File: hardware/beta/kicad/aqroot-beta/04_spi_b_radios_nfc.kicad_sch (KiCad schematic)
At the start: 0 parts

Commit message: AQROOT Beta: capture SPI-B radios and NFC architecture
Completes sheet 04, bringing all three SPI Bus B devices into the
schematic against the functional placeholder symbols added in 5e4471a,
ba2be78 and 1f152bd. Bus B is now the shared SPI_B_SCK / SPI_B_MOSI /
SPI_B_MISO bus with one chip select per device.

CC1101 -- AQROOT_Beta:CC1101_RADIO_PLACEHOLDER
  CC1101_CS_N, CC1101_GDO0, CC1101_RF_TBD, 100nF decoupling,
  10k hardware pull-up on CC1101_CS_N.

SX1262 -- AQROOT_Beta:SX1262_MODULE_PLACEHOLDER
  SX1262_CS_N, SX1262_BUSY, SX1262_DIO1, SX1262_RST_N (from expander
  U60 P01), SX1262_RF_TBD, 100nF decoupling, 10k hardware pull-up on
  SX1262_CS_N.

ST25R3916 -- AQROOT_Beta:ST25R3916_NFC_PLACEHOLDER
  VDD_IO_3V3 and VDD_DIG_3V3 to +3V3, VDD_PA_5V to NFC_5V_PA_PENDING
  (the switched 5V PA rail, boost IC unresolved). NFC_CS_N, NFC_IRQ,
  and the RF and clock ports NFC_RFO1/RFO2/RFI1/RFI2_TBD and
  NFC_XIN/XOUT_TBD. 10k hardware pull-up on NFC_CS_N, plus provisional
  100nF placeholders on +3V3 and on NFC_5V_PA_PENDING.

Passives placed: C16, C17 (100nF), C18, C19 (100nF_PLACEHOLDER),
R27, R28, R29 (10k CS pull-ups).

Root sheet exposes and labels SPI_B_SCK, SPI_B_MOSI, SPI_B_MISO,
CC1101_CS_N, CC1101_GDO0, SX1262_CS_N, SX1262_BUSY, SX1262_DIO1,
SX1262_RST_N, NFC_CS_N and NFC_IRQ.

All three parts carry a blank Footprint and on_board=no, and the sheet
carries DO NOT ROUTE notes. Nothing here is routable: the CC1101
module-vs-bare-IC choice, the SX1262 certified module (Ebyte E22 vs
Waveshare Core1262), and the ST25R3916 package, support networks, coil
and matching all remain unresolved. Every _TBD and _PENDING net name is
deliberate and must be replaced before layout.

Also in this commit, both rewritten by KiCad during the same session:
  - aqroot-Beta.kicad_pro: ERC pin_to_pin severity raised from warning
    to error, and used_designators updated by the annotator.
  - 03_spi_a_display_sd.kicad_sch: two pin UUIDs regenerated on save;
    no connectivity or compon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
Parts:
- added C16, C17: 100nF, symbol Device:C
- added C18, C19: 100nF_PLACEHOLDER, symbol Device:C
- added R27, R28, R29: 10k, symbol Device:R
- added U7: CC1101_RADIO_PLACEHOLDER, symbol AQROOT_Beta:CC1101_RADIO_PLACEHOLDER
- added U8: SX1262_MODULE_PLACEHOLDER, symbol AQROOT_Beta:SX1262_MODULE_PLACEHOLDER
- added U9: ST25R3916_NFC_PLACEHOLDER, symbol AQROOT_Beta:ST25R3916_NFC_PLACEHOLDER
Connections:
- new net +3V3: C16.1, C17.1, C18.1, R27.1, R28.1, R29.1, U7.1 (VCC_3V3), U8.1 (VCC_3V3), U9.1 (VDD_IO_3V3), U9.2 (VDD_DIG_3V3)
- new net CC1101_CS_N: R28.2, U7.6 (CS_N)
- new net CC1101_GDO0: U7.7 (GDO0)
- new net CC1101_RF_TBD: U7.8 (RF_ANT)
- new net GND: C16.2, C17.2, C18.2, C19.2, U7.2 (GND), U8.2 (GND), U9.4 (GND)
- new net NFC_5V_PA_PENDING: C19.1, U9.3 (VDD_PA_5V)
- new net NFC_CS_N: R29.2, U9.8 (CS_N)
- new net NFC_IRQ: U9.9 (IRQ)
- new net NFC_RFI1_TBD: U9.12 (RFI1)
- new net NFC_RFI2_TBD: U9.13 (RFI2)
- new net NFC_RFO1_TBD: U9.10 (RFO1)
- new net NFC_RFO2_TBD: U9.11 (RFO2)
- new net NFC_XIN_TBD: U9.14 (XIN)
- new net NFC_XOUT_TBD: U9.15 (XOUT)
- new net SPI_B_MISO: U7.5 (MISO), U8.5 (MISO), U9.7 (MISO)
- new net SPI_B_MOSI: U7.4 (MOSI), U8.4 (MOSI), U9.6 (MOSI)
- new net SPI_B_SCK: U7.3 (SCK), U8.3 (SCK), U9.5 (SCK)
- new net SX1262_BUSY: U8.7 (BUSY)
- new net SX1262_CS_N: R27.2, U8.6 (CS_N)
- new net SX1262_DIO1: U8.8 (DIO1)
- new net SX1262_RF_TBD: U8.10 (RF_ANT)
- new net SX1262_RST_N: U8.9 (RESET_N)
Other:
- note added: "CC1101 FUNCTIONAL PLACEHOLDER MODULE / BARE-IC IMPLEMENTATION PENDING RF MATCHING / FILTERING / ANTENNA INTERFACE PENDING GDO2 INTENTIONALLY OMITTED CS HAS 10k HARDWARE PULL-UP TO +3V3 NO FOOTPRINT DO NOT ROUTE"
- note added: "SPI BUS B - BETA BRING-UP RISK THREE SHARED DEVICES: CC1101 + SX1262 + ST25R3916 ALL THREE CS LINES HAVE HARDWARE PULL-UPS ST25R3916 WAS VALIDATED STANDALONE ON ALPHA NFC AS THIRD BUS-B DEVICE IS FIRST VALIDATED ON BETA FIRMWARE MUST: - DRIVE ALL CS HIGH BEFORE INITIALIZATION - USE A BUS MUTEX - SET SPI MODE / FREQUENCY PER TRANSACTION - VERIFY NO DEVICE HOLDS MISO DO NOT ROUTE NFC UNTIL PACKAGE,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"
- note added: "SX1262 FUNCTIONAL PLACEHOLDER EXACT CERTIFIED MODULE PENDING EBYTE E22 VS WAVESHARE CORE1262 UNRESOLVED RF / ANTENNA INTERFACE PENDING CS HAS 10k HARDWARE PULL-UP TO +3V3 RESET SAFE-STATE CONTROLLED BY U60 P01 NO FOOTPRINT DO NOT ROUTE"

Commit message: Schematics: root connectivity pass for XGPIO, I2C_SDA_INT and NFC_5V_PA_PENDING
Work-in-progress checkpoint of the root-level connectivity pass. Verified with
kicad-cli netlist and ERC comparison against the previous commit.

Resolved:
- NFC_5V_PA_PENDING was split across two isolated sheet-local nets,
  /01_POWER_TREE/NFC_5V_PA_PENDING (C34.2 C35.1 R44.2 TP9.1 U13.6) and
  /04_SPI_B_RADIOS_NFC/NFC_5V_PA_PENDING (C19.1 alone). Promoted the local
  label in 04_spi_b_radios_nfc to a hierarchical input label, added the
  matching sheet pin on the root, and extended the wire to reach it. These
  now form a single root net /NFC_5V_PA_PENDING with all 6 nodes.
- I2C_SDA_INT: U14.8 was stranded on its own sheet-local net. It now joins
  the main /I2C_SDA_INT net (6 -> 7 nodes).
- ERC pin_not_connected: 77 -> 56 (21 pins newly connected).

Known incomplete, to be finished in a follow-up:
- 18 newly placed root labels are dangling because their wiring is not yet
  drawn: XGPIO0..XGPIO14, ACC_PWR_EN, FAST_IO_U0TXD_ROOTPROBE_CS, WAKE_INT_N.
  ERC label_dangling: 39 -> 57.
- REGRESSION: WAKE_INT_N lost U1.23 (MCU wake input). The root wire from
  (152.4, 24.13) to (152.4, 26.67) was removed, which disconnected the
  WAKE_INT_N label from the 02_MCU_CORE sheet pin at (152.4, 25.4). The net
  dropped from 4 nodes (R3.1 U1.23 U2.1 U3.1) to 3, and U1.23 is now an
  isolated /02_MCU_CORE/WAKE_INT_N. This must be reconnected before the
  netlist is used for layout.

Also clears the stale used_designators cache in the project file, a side
effect of the KiCad editing session.

No symbol, footprint, PCB or library-table changes.

Co-Authored-By: Claude Opus 5 <noreply@anthropic.com>
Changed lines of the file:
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@@
-	(wire
-		(pts
-			(xy 104.14 129.54) (xy 104.14 130.81)
-		)
-		(stroke
-			(width 0)
-			(type default)
-		)
-	)
 	(wire
 		(pts
@@
 		(pts
 			(xy 66.04 52.07) (xy 67.31 52.07)
+		)
+		(stroke
+			(width 0)
+			(type default)
+		)
+	)
+	(wire
+		(pts
+			(xy 104.14 128.27) (xy 104.14 130.81)
 		)
 		(stroke
@@
 			)
 			(justify right bottom)
-		)
-	)
-	(label "NFC_5V_PA_PENDING"
-		(at 104.14 129.54 90)
-		(effects
-			(font
-				(size 1.27 1.27)
-			)
-			(justify left bottom)
 		)
 	)
@@
 		)
 	)
+	(hierarchical_label "NFC_5V_PA_PENDING"
+		(shape input)
+		(at 104.14 128.27 90)
+		(effects
+			(font
+				(size 1.27 1.27)
+			)
+			(justify left)
+		)
+	)

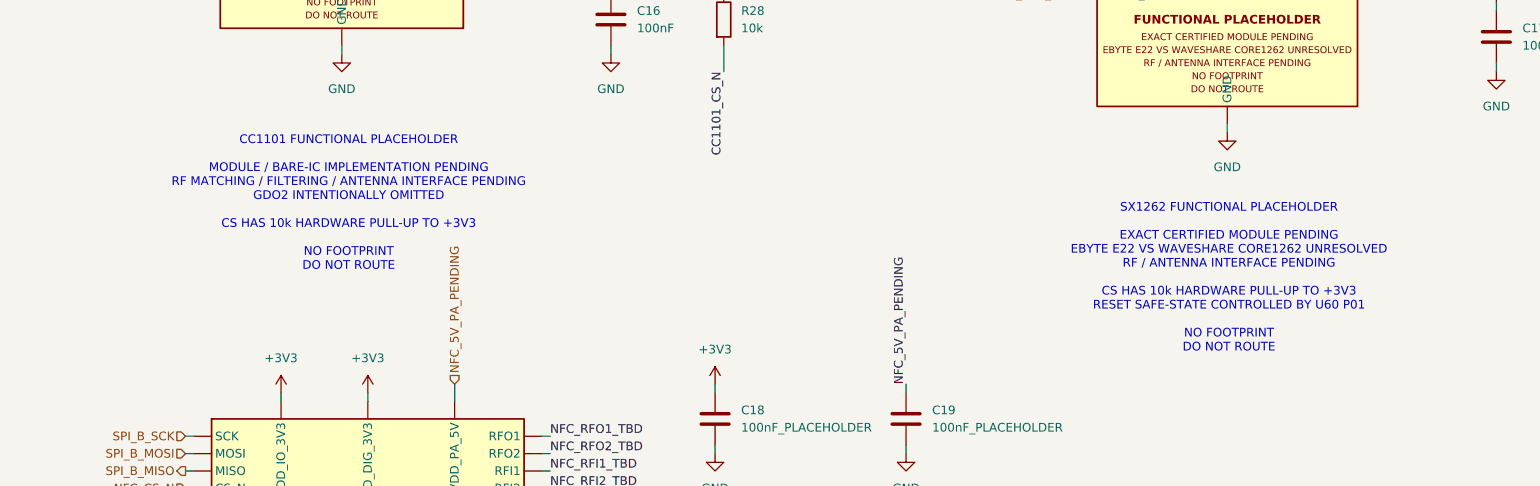
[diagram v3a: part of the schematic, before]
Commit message: schematic: update SPI Bus B radio sheet text for module lock (E22-900M22S + E07-400M10S)
Sheet annotations only. Symbol body graphics still carry the stale text and are
unchanged - those live in the lib_symbols cache and mirror AQROOT_Beta.kicad_sym,
so they must be edited together in the symbol editor.

Co-Authored-By: Claude Opus 5 <noreply@anthropic.com>
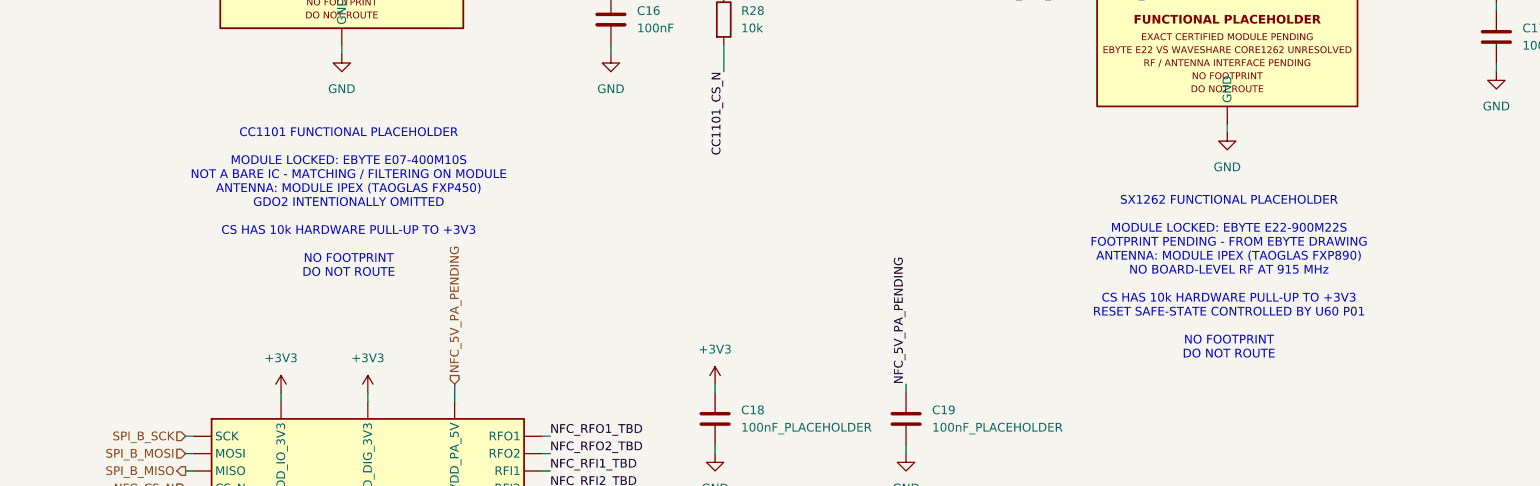
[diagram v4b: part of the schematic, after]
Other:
- note added: "CC1101 FUNCTIONAL PLACEHOLDER MODULE LOCKED: EBYTE E07-400M10S NOT A BARE IC - MATCHING / FILTERING ON MODULE ANTENNA: MODULE IPEX (TAOGLAS FXP450) GDO2 INTENTIONALLY OMITTED CS HAS 10k HARDWARE PULL-UP TO +3V3 NO FOOTPRINT DO NOT ROUTE"
- note added: "SX1262 FUNCTIONAL PLACEHOLDER MODULE LOCKED: EBYTE E22-900M22S FOOTPRINT PENDING - FROM EBYTE DRAWING ANTENNA: MODULE IPEX (TAOGLAS FXP890) NO BOARD-LEVEL RF AT 915 MHz CS HAS 10k HARDWARE PULL-UP TO +3V3 RESET SAFE-STATE CONTROLLED BY U60 P01 NO FOOTPRINT DO NOT ROUTE"
- note removed: "CC1101 FUNCTIONAL PLACEHOLDER MODULE / BARE-IC IMPLEMENTATION PENDING RF MATCHING / FILTERING / ANTENNA INTERFACE PENDING GDO2 INTENTIONALLY OMITTED CS HAS 10k HARDWARE PULL-UP TO +3V3 NO FOOTPRINT DO NOT ROUTE"
- note removed: "SX1262 FUNCTIONAL PLACEHOLDER EXACT CERTIFIED MODULE PENDING EBYTE E22 VS WAVESHARE CORE1262 UNRESOLVED RF / ANTENNA INTERFACE PENDING CS HAS 10k HARDWARE PULL-UP TO +3V3 RESET SAFE-STATE CONTROLLED BY U60 P01 NO FOOTPRINT DO NOT ROUTE"
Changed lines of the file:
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@@
 	(generator_version "10.0")
 	(paper "A4")
-	(text "CC1101 FUNCTIONAL PLACEHOLDER\n\nMODULE / BARE-IC IMPLEMENTATION PENDING\nRF MATCHING / FILTERING / ANTENNA INTERFACE PENDING\nGDO2 INTENTIONALLY OMITTED\n\nCS HAS 10k HARDWARE PULL-UP TO +3V3\n\nNO FOOTPRINT\nDO NOT ROUTE"
+	(text "CC1101 FUNCTIONAL PLACEHOLDER\n\nMODULE LOCKED: EBYTE E07-400M10S\nNOT A BARE IC - MATCHING / FILTERING ON MODULE\nANTENNA: MODULE IPEX (TAOGLAS FXP450)\nGDO2 INTENTIONALLY OMITTED\n\nCS HAS 10k HARDWARE PULL-UP TO +3V3\n\nNO FOOTPRINT\nDO NOT ROUTE"
 		(exclude_from_sim no)
 		(at 88.646 101.854 0)
@@
 		)
 	)
-	(text "SX1262 FUNCTIONAL PLACEHOLDER\n\nEXACT CERTIFIED MODULE PENDING\nEBYTE E22 VS WAVESHARE CORE1262 UNRESOLVED\nRF / ANTENNA INTERFACE PENDING\n\nCS HAS 10k HARDWARE PULL-UP TO +3V3\nRESET SAFE-STATE CONTROLLED BY U60 P01\n\nNO FOOTPRINT\nDO NOT ROUTE"
+	(text "SX1262 FUNCTIONAL PLACEHOLDER\n\nMODULE LOCKED: EBYTE E22-900M22S\nFOOTPRINT PENDING - FROM EBYTE DRAWING\nANTENNA: MODULE IPEX (TAOGLAS FXP890)\nNO BOARD-LEVEL RF AT 915 MHz\n\nCS HAS 10k HARDWARE PULL-UP TO +3V3\nRESET SAFE-STATE CONTROLLED BY U60 P01\n\nNO FOOTPRINT\nDO NOT ROUTE"
 		(exclude_from_sim no)
 		(at 217.424 112.776 0)
